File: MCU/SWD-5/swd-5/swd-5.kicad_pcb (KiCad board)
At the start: 2 copper layers, 11.4 x 8.6 mm, 3 parts, among them J1-A1 SWD-5, J1-B1 SWD-5, J2 SWD-10

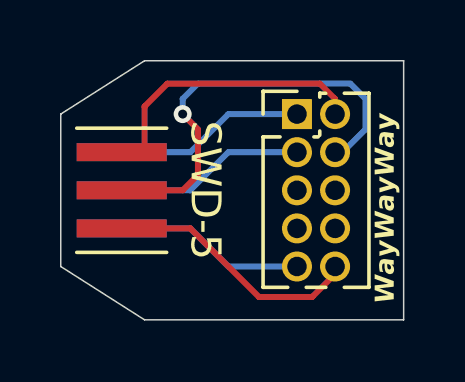
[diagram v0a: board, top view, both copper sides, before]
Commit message: Redone Z-input PCB; production update
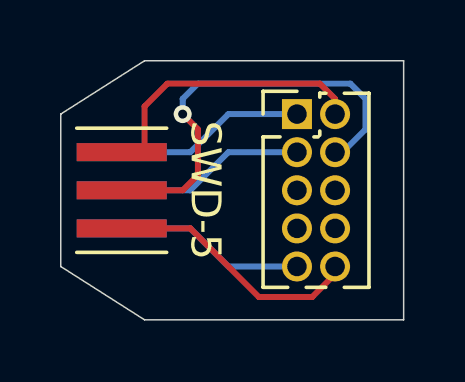
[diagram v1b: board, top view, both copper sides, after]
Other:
- board text removed: "WayWayWay"
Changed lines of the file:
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@@
 		(at 70.104 66.04 -90)
 		(property "Reference" "J1-B1"
-			(at 0.762 -2.794 270)
+			(at 0.762 -2.794 -90)
 			(unlocked yes)
 			(layer "F.SilkS")
@@
 		)
 		(property "Value" "SWD-5"
-			(at 0 -2.794 270)
+			(at 0 -2.794 -90)
 			(unlocked yes)
 			(layer "F.SilkS")
@@
 		)
 	)
-	(gr_text "WayWayWay"
-		(at 79.248 63.5 90)
-		(layer "F.SilkS")
-		(effects
-			(font
-				(size 0.635 0.635)
-				(thickness 0.1524)
-				(bold yes)
-				(italic yes)
-			)
-			(justify right bottom)
-		)
-	)
